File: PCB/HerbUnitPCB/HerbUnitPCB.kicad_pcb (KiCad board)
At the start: 2 copper layers, 39 parts, among them J1 USB_C_Receptacle_USB2.0_16P, J2 Barrel_Jack_Switch_Pin3Ring, J4 SD_Card_Device, SW1 SW_Push, SW2 SW_Push, SW3 SW_Push, U1 USBLC6-2P6, U2 ESP32-S3-WROOM-1, U3 AMS1117-5.0, U5 DHT11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

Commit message: Arranged components
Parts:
- added J3: Conn_01x03_Pin, Connector_PinHeader_2.54mm:PinHeader_1x03_P2.54mm_Horizontal, F.Cu at (150.2, 55.0)
- added J5: Screw_Terminal_01x02, TerminalBlock_Philmore:TerminalBlock_Philmore_TB132_1x02_P5.00mm_Horizontal, F.Cu at (145.6, 38.6)
- added J6: Conn_01x03_Pin, Connector_PinHeader_2.54mm:PinHeader_1x03_P2.54mm_Horizontal, F.Cu at (150.4, 65.5)
- added R1: 0, Resistor_SMD:R_0805_2012Metric, F.Cu at (165.1, 80.2)
- C1, C3, C4, C5, C6, C7: footprint Capacitor_SMD:C_0402_1005Metric -> Capacitor_SMD:C_0805_2012Metric
- D2, D3, D4: footprint LED_SMD:LED_0201_0603Metric -> LED_SMD:LED_1210_3225Metric_Pad1.42x2.65mm_HandSolder
- R14, R9: footprint Resistor_SMD:R_0402_1005Metric -> Resistor_SMD:R_0805_2012Metric
- moved U2 112.4 mm to (170.8, 41.6)
- moved R11 90.2 mm to (204.2, 83.6), turned to -90 degrees
- moved J2 88.5 mm to (146.6, 81.1), turned to 90 degrees
- moved SW3 84.9 mm to (213.4, 80.0), turned to -90 degrees
- moved R5 84.0 mm to (180.3, 82.3)
- moved R4 82.6 mm to (178.3, 82.3)
- moved R7 82.3 mm to (180.8, 74.7)
- moved R6 80.6 mm to (178.8, 74.7)
- moved R2 75.8 mm to (169.4, 83.3), turned to -90 degrees
- moved R13 72.8 mm to (186.9, 84.3)
- moved U3 72.5 mm to (145.8, 73.5), turned to 90 degrees
- moved R10 72.3 mm to (186.9, 76.7)
- moved R12 72.2 mm to (186.9, 80.5)
- moved R3 71.5 mm to (165.6, 83.3), turned to 90 degrees
- moved J4 57.7 mm to (198.6, 51.8), turned to 90 degrees
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
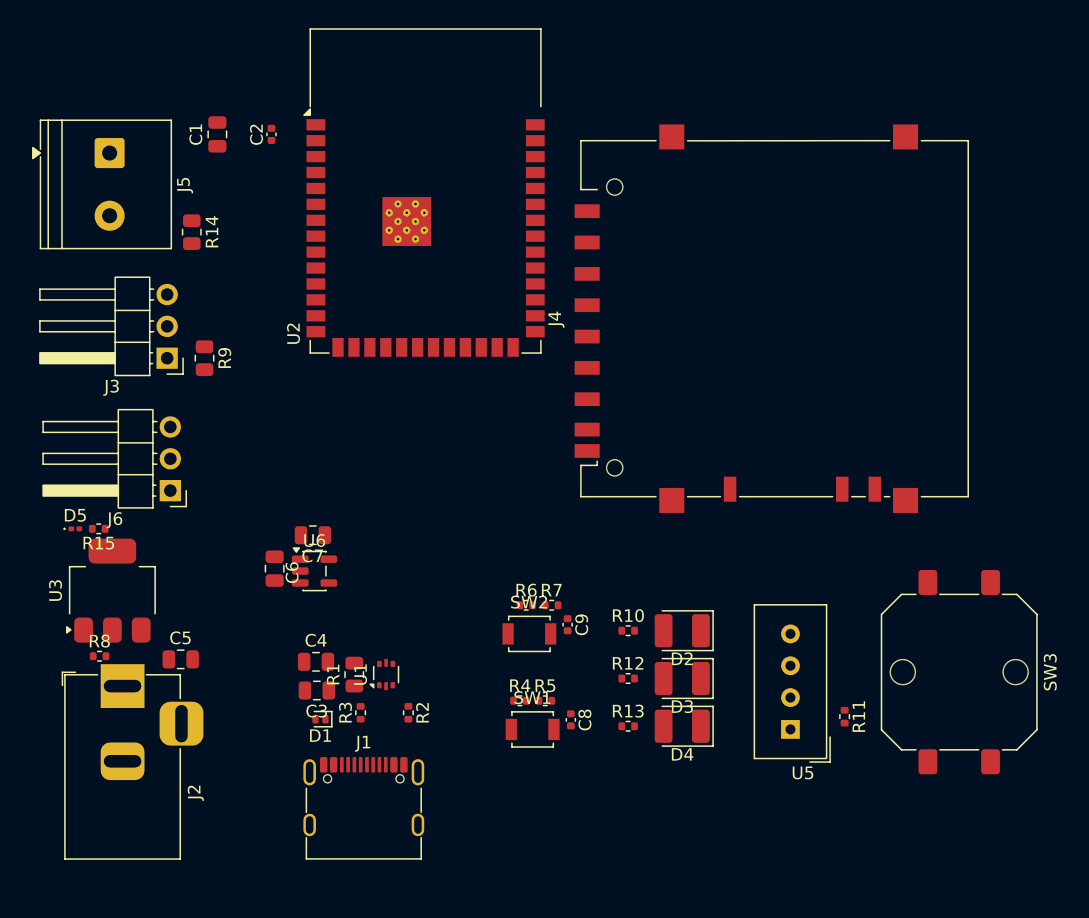
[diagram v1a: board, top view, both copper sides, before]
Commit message: Experimented with component arrangement again
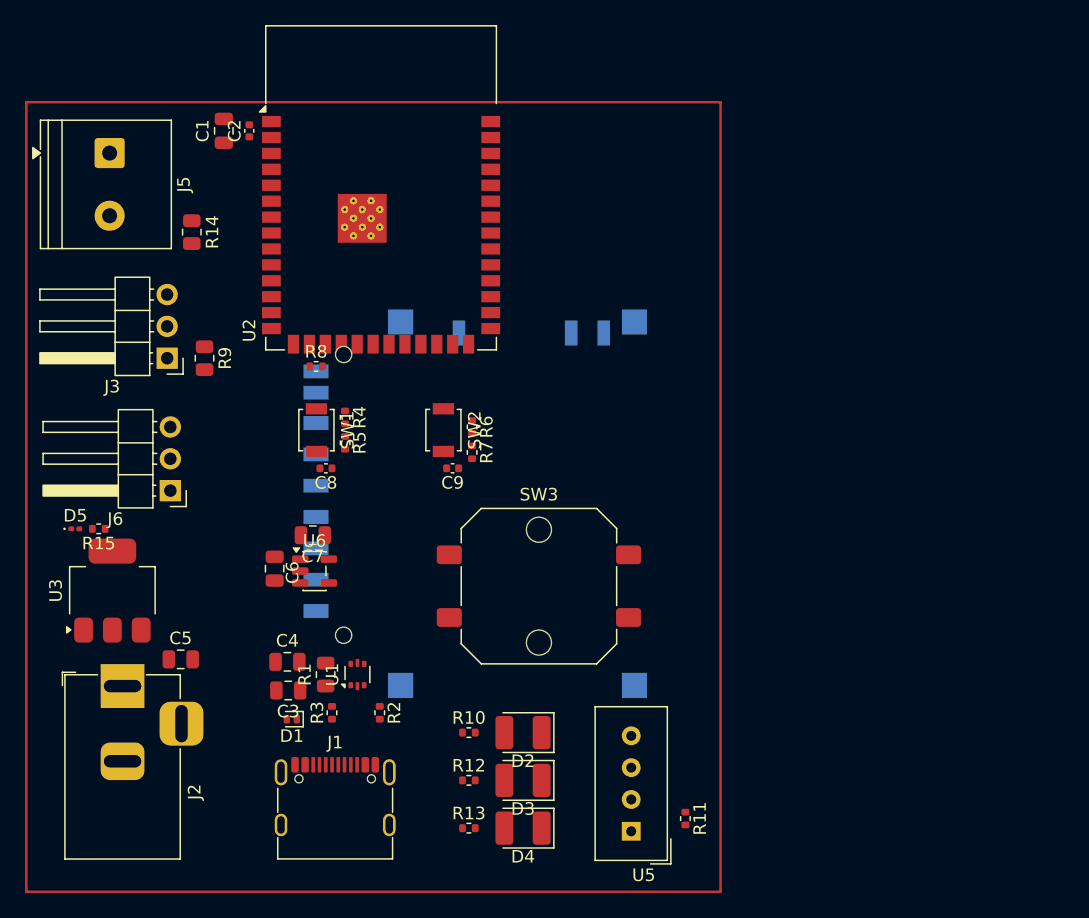
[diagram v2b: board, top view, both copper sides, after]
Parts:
- J4: moved to B.Cu
- moved SW3 34.2 mm to (179.8, 73.2), turned to 0 degrees
- moved SW1 29.5 mm to (162.1, 60.7), turned to -90 degrees
- moved R8 28.9 mm to (162.1, 55.6)
- moved C8 28.0 mm to (162.8, 63.8), turned to 180 degrees
- moved R4 26.6 mm to (164.4, 59.7), turned to -90 degrees
- moved J4 26.2 mm to (177.0, 66.6), turned to -90 degrees
- moved R5 26.1 mm to (164.4, 61.7), turned to -90 degrees
- moved SW2 17.6 mm to (172.2, 60.7), turned to -90 degrees
- moved C9 15.5 mm to (172.9, 63.8), turned to 180 degrees
- moved D2 15.1 mm to (178.6, 84.8)
- moved D3 15.1 mm to (178.6, 88.6)
- moved D4 15.1 mm to (178.6, 92.5)
- moved R10 15.1 mm to (174.2, 84.8)
- moved R11 15.1 mm to (191.5, 91.7)
- moved R12 15.1 mm to (174.2, 88.6)
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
